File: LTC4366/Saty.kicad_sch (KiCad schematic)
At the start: 12 parts, among them J1 Conn_01x02, Q1 HUF76639S3S

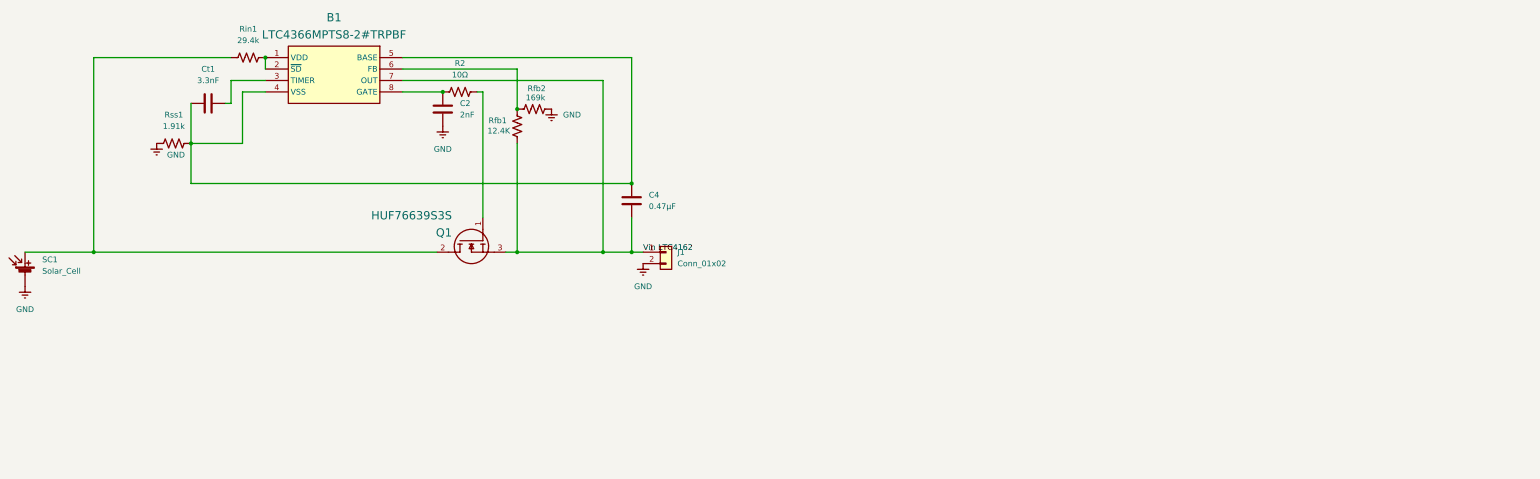
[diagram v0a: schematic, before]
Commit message: update the pcb layout of LTC4366
fixes clearance
fixes length
fixes track width
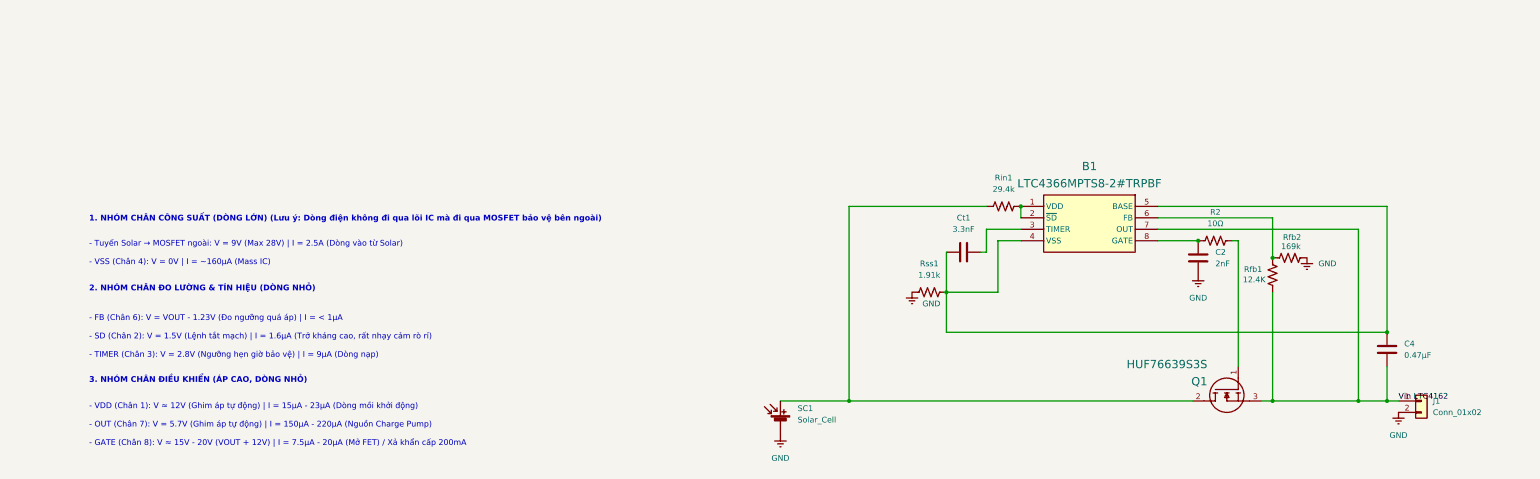
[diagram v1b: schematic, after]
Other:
- note added: "- FB (Chân 6): V = VOUT - 1.23V (Đo ngưỡng quá áp) | I = < 1µA - SD (Chân 2): V = 1.5V (Lệnh tắt mạch) | I = 1.6µA (Trở kháng cao, rất nhạy cảm rò rỉ) - TIMER (Chân 3): V = 2.8V (Ngưỡng hẹn giờ bảo vệ) | I = 9µA (Dòng nạp)"
- note added: "- Tuyến Solar → MOSFET ngoài: V = 9V (Max 28V) | I = 2.5A (Dòng vào từ Solar) - VSS (Chân 4): V = 0V | I = ~160µA (Mass IC)"
- note added: "- VDD (Chân 1): V ≈ 12V (Ghim áp tự động) | I = 15µA - 23µA (Dòng mồi khởi động) - OUT (Chân 7): V = 5.7V (Ghim áp tự động) | I = 150µA - 220µA (Nguồn Charge Pump) - GATE (Chân 8): V ≈ 15V - 20V (VOUT + 12V) | I = 7.5µA - 20µA (Mở FET) / Xả khẩn cấp 200mA"
- note added: "1. NHÓM CHÂN CÔNG SUẤT (DÒNG LỚN) (Lưu ý: Dòng điện không đi qua lõi IC mà đi qua MOSFET bảo vệ bên ngoài)"
- note added: "2. NHÓM CHÂN ĐO LƯỜNG & TÍN HIỆU (DÒNG NHỎ)"
- note added: "3. NHÓM CHÂN ĐIỀU KHIỂN (ÁP CAO, DÒNG NHỎ)"
- moved on the sheet: B1, C2, C4, Ct1, J1, Q1, R2, Rfb1, Rfb2, Rin1, Rss1, SC1

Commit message: Add files via upload
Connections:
- net GND: now also J1.1 (Pin_1); no longer J1.2 (Pin_2)
- net Vin LTC4162: now also J1.2 (Pin_2); no longer J1.1 (Pin_1)
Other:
- moved on the sheet: B1, C2, C4, Ct1, J1, Q1, R2, Rfb1, Rfb2, Rin1, Rss1, SC1
